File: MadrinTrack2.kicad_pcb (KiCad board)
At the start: 4 copper layers, 18 parts, among them J1 Jumper_NC_Small, Q1 2N7000, U1 DWM1001, U2 MCP73831-2-OT, U3 ESP-12E

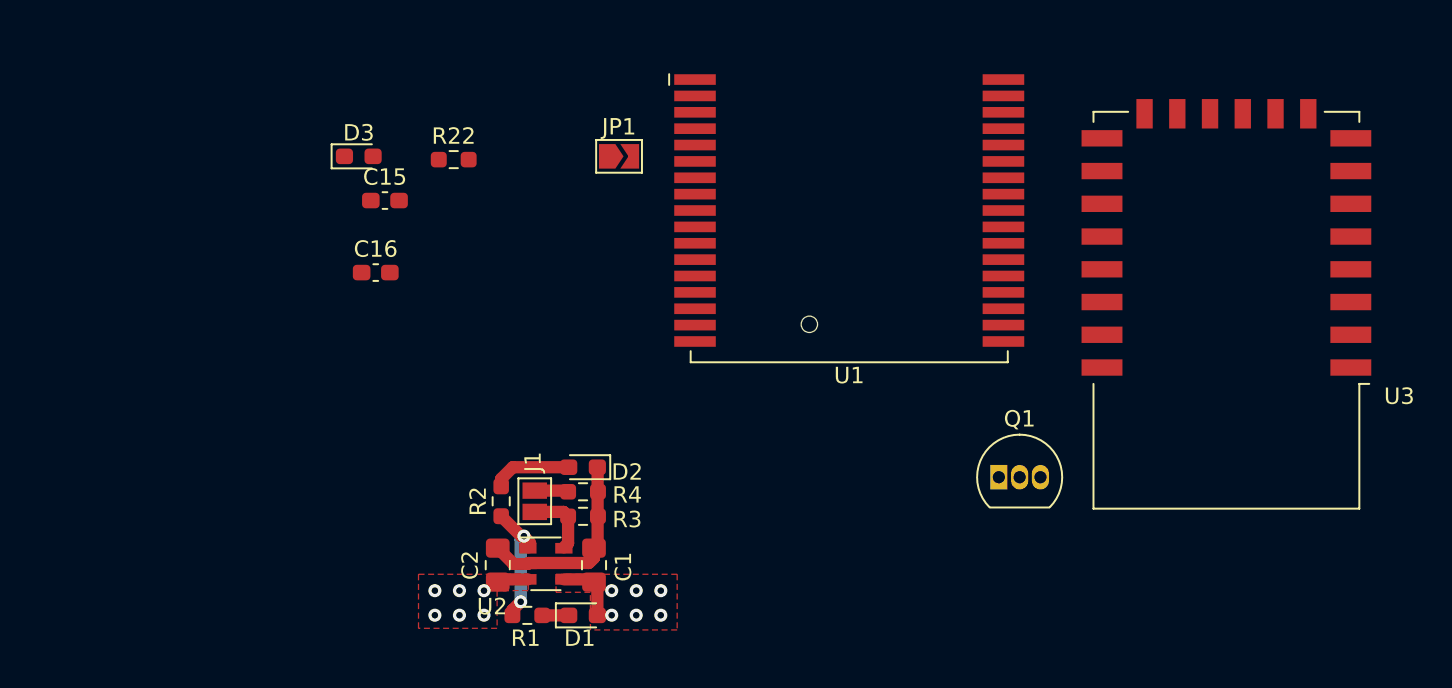
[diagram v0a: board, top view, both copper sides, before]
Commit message: adding fiducial
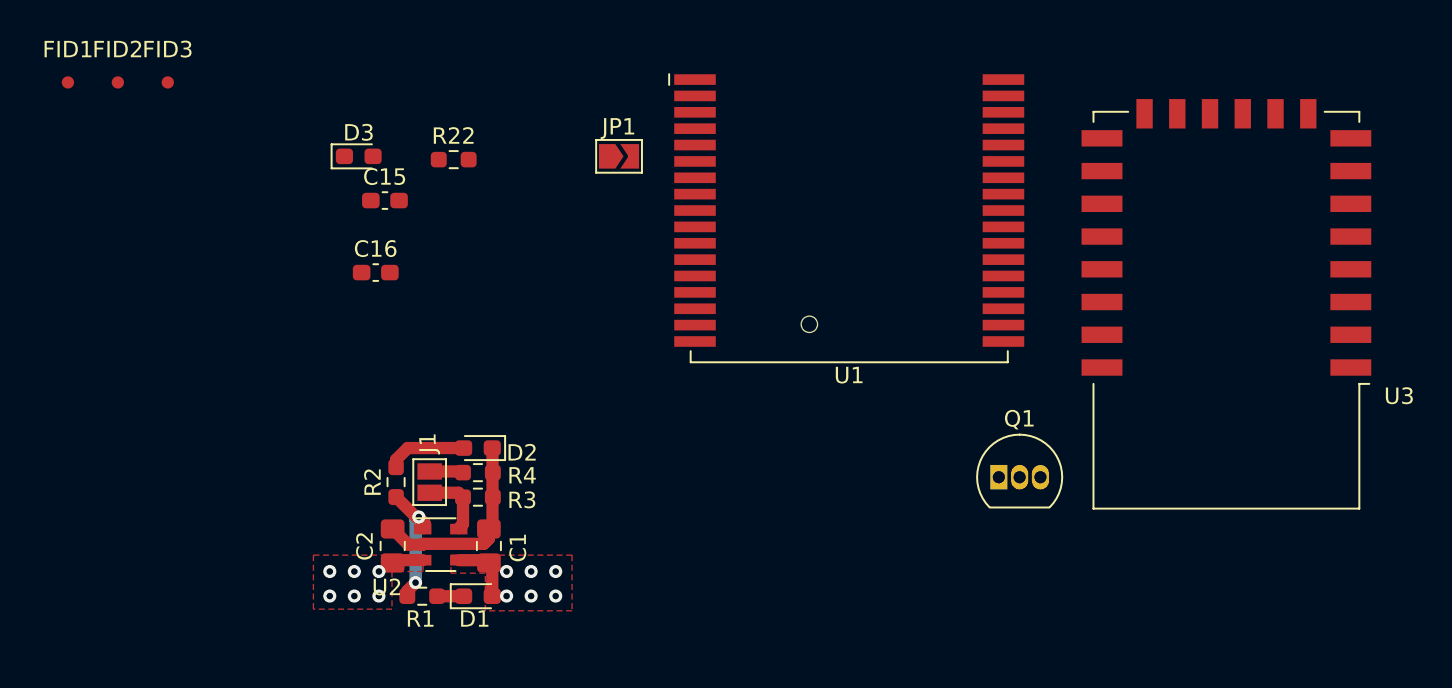
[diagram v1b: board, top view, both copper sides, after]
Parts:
- added FID1: Fiducial, Fiducial:Fiducial_0.75mm_Mask1.5mm, F.Cu at (76.5, 111.8)
- added FID2: Fiducial, Fiducial:Fiducial_0.75mm_Mask1.5mm, F.Cu at (79.6, 111.8)
- added FID3: Fiducial, Fiducial:Fiducial_0.75mm_Mask1.5mm, F.Cu at (82.6, 111.8)
- moved C1 6.53 mm to (102.2, 140.1)
- moved C2 6.53 mm to (96.4, 140.1)
- moved D1 6.53 mm to (101.6, 143.2)
- moved J1 6.53 mm to (98.6, 136.2)
- moved R1 6.53 mm to (98.2, 143.2)
- moved R2 6.53 mm to (96.6, 136.2)
- moved D2 6.53 mm to (101.6, 134.1)
- moved R3 6.53 mm to (101.6, 137.1)
- moved R4 6.53 mm to (101.6, 135.6)
- moved U2 6.53 mm to (99.3, 140.0)
